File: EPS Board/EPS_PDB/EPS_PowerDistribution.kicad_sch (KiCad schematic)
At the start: 26 parts, among them U10 TPS259621DDAT, U11 LTC3624IDD-25PBF, U12 TPS259621DDAT, U13 TPS259621DDAT, U6 TPS259621DDAT, U7 TPS259621DDAT, U9 TPS259621DDAT

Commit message: Power Distri & Reg Schematic Complete
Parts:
- added C23, C24: 10uF, Capacitor_SMD:C_0805_2012Metric_Pad1.18x1.45mm_HandSolder, symbol Device:C_Small
- added C25, C27, C28: TBD, Capacitor_SMD:C_0805_2012Metric_Pad1.18x1.45mm_HandSolder, symbol Device:C_Small
- added C26: 0.47uF, Capacitor_SMD:C_0805_2012Metric_Pad1.18x1.45mm_HandSolder, symbol Device:C_Small
- added D3: D, symbol Device:D
- added JP2, JP3: ~, symbol Jumper:Jumper_3_Bridged12
- added L3: 16uH, Inductor_SMD:L_0805_2012Metric_Pad1.15x1.40mm_HandSolder, symbol Device:L
- added R29: 510, Resistor_SMD:R_0603_1608Metric_Pad0.98x0.95mm_HandSolder, symbol EPS_Schematic_v2-eagle-import:R-USCHIP-0805(2012-METRIC)
- added R30: 2.2k, Resistor_SMD:R_0603_1608Metric_Pad0.98x0.95mm_HandSolder, symbol EPS_Schematic_v2-eagle-import:R-USCHIP-0805(2012-METRIC)
- added R31: 10k, Resistor_SMD:R_0603_1608Metric_Pad0.98x0.95mm_HandSolder, symbol EPS_Schematic_v2-eagle-import:R-USCHIP-0805(2012-METRIC)
- added R32: 400k, Resistor_SMD:R_0603_1608Metric_Pad0.98x0.95mm_HandSolder, symbol EPS_Schematic_v2-eagle-import:R-USCHIP-0805(2012-METRIC)
- added R33: TBD, Resistor_SMD:R_0603_1608Metric_Pad0.98x0.95mm_HandSolder, symbol EPS_Schematic_v2-eagle-import:R-USCHIP-0805(2012-METRIC)
- added R34: 10, Resistor_SMD:R_0603_1608Metric_Pad0.98x0.95mm_HandSolder, symbol EPS_Schematic_v2-eagle-import:R-USCHIP-0805(2012-METRIC)
- added R35: 130k, Resistor_SMD:R_0603_1608Metric_Pad0.98x0.95mm_HandSolder, symbol EPS_Schematic_v2-eagle-import:R-USCHIP-0805(2012-METRIC)
- added R36: 15k, Resistor_SMD:R_0603_1608Metric_Pad0.98x0.95mm_HandSolder, symbol EPS_Schematic_v2-eagle-import:R-USCHIP-0805(2012-METRIC)
- added U14, U15, U16: TPS259621DDAT, EPS_Schematic_v2:IC_TPS259621DDAT, symbol TPS259621DDAT:TPS259621DDAT
- added U17: LM5000-3MTCX, LM5000-3MTCX:SOP65P640X120-16N, symbol LM5000-3MTCX:LM5000-3MTCX
- R14: value 510 -> 560
- R18, R21: value R-USCHIP-0805(2012-METRIC) -> 560
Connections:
- net ADCS_3.3V_EN is gone; now on net 3.3V_bus: U13.3 (EN/UVLO)
- net 12V_bus: now also C28.2, D3.1 (K), R35.1
- net 3.3V_bus: now also U8.8 (FB), U15.4 (IN), U16.4 (IN)
- net 5V_bus: now also U14.4 (IN)
- net GND: now also U8.11 (GND), U8.12 (GND), C23.1, C24.1, C26.1, C27.1, C28.1, JP2.1 (A), JP3.1 (A), R29.1, R30.1, R31.1, R32.2, R33.2, R36.1, U14.1 (GND), U14.9 (EXP), U15.1 (GND), U15.8 (OVCSEL), U15.9 (EXP), U16.1 (GND), U16.8 (OVCSEL), U16.9 (EXP), U17.16 (TEST), U17.4 (AGND), U17.5 (PGND-1), U17.6 (PGND), U17.7 (PGND-3), U17.8 (PGND-2); no longer C19.1
- net at C22.2, U11.6 (INTVCC): now also JP2.3 (B)
- net at U11.7 (MODE/SYNC): now also JP2.2 (C)
- net at L1.2: now also U8.1 (SW), U8.2 (SW)
- net at C17.2: now also U8.9 (INTVCC), JP3.3 (B)
- net VBUS: now reaches C21.1
- net VBUS: now also C19.1, L3.1, R34.2
- net at C19.2: now also U8.3 (Vin), U8.4 (Vin), U8.5 (RUN)
- net at U8.10 (MODE/SYNC): now also JP3.2 (C)
- net 3V3_STATUS: now reaches U8.6 (PGOOD)
- net 5V_PGOOD renamed 5V_STATUS
- net ADCS_12V renamed 12V_ADCS
- net ADCS_12V_EN renamed EN_12V_ADCS
- net ADCS_12V_FLT renamed FLT_12V_ADCS
- net ADCS_3.3V renamed 3V3_EPS
- net ADCS_3.3V_FLT renamed FLT_3V3_EPS
- net ADCS_5V renamed 5V_ADCS
- net ADCS_5V_EN renamed EN_5V_ADCS
- net ADCS_5V_FLT renamed FLT_5V_ADCS
- net COMM_5V renamed 5V_COMM
- net COMM_5V_EN renamed EN_5V_COMM
- net COMM_5V_FLT renamed FLT_5V_COMM
- net EPS_5V renamed 5V_EPS
- net EPS_5V_EN renamed EN_5V_EPS
- net EPS_5V_FLT renamed FLT_5V_EPS
- net OBC_5V renamed 5V_OBC
- net OBC_5V_EN renamed EN_5V_OBC
- net OBC_5V_FLT renamed FLT_5V_OBC
- new net: C25.1, R33.1
- new net: C24.2, C25.2, U17.1 (COMP)
- new net: R35.2, R36.2, U17.2 (FB)
- new net: R32.1, U14.8 (OVCSEL)
- new net: R30.2, U15.7 (ILM)
- new net: D3.2 (A), L3.2, U17.10 (SW), U17.11 (SW-2), U17.9 (SW-1)
- new net: C23.2, U17.12 (BYP)
- new net: C26.2, R34.1, U17.13 (VIN)
- new net: C27.2, U17.14 (SS)
- new net: R29.2, U14.7 (ILM)
- new net: R31.2, U16.7 (ILM)
- new net 12V_SHDN: U17.3 (SHDN)
- new net 3V3_ADCS: U15.5 (OUT)
- new net 3V3_ANT: U16.5 (OUT)
- new net 5V_PAY: U14.5 (OUT)
- new net EN_3V3_ADCS: U15.3 (EN/UVLO)
- new net EN_3V3_ANT: U16.3 (EN/UVLO)
- new net EN_5V_PAY: U14.3 (EN/UVLO)
- new net FLT_3V3_ADCS: U15.6 (~{FLT})
- new net FLT_3V3_ANT: U16.6 (~{FLT})
- new net FLT_5V_PAY: U14.6 (~{FLT})
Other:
- moved on the sheet: C17, C18, C19, C20, C21, C22, L1, L2, R13, R14, R15, R16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

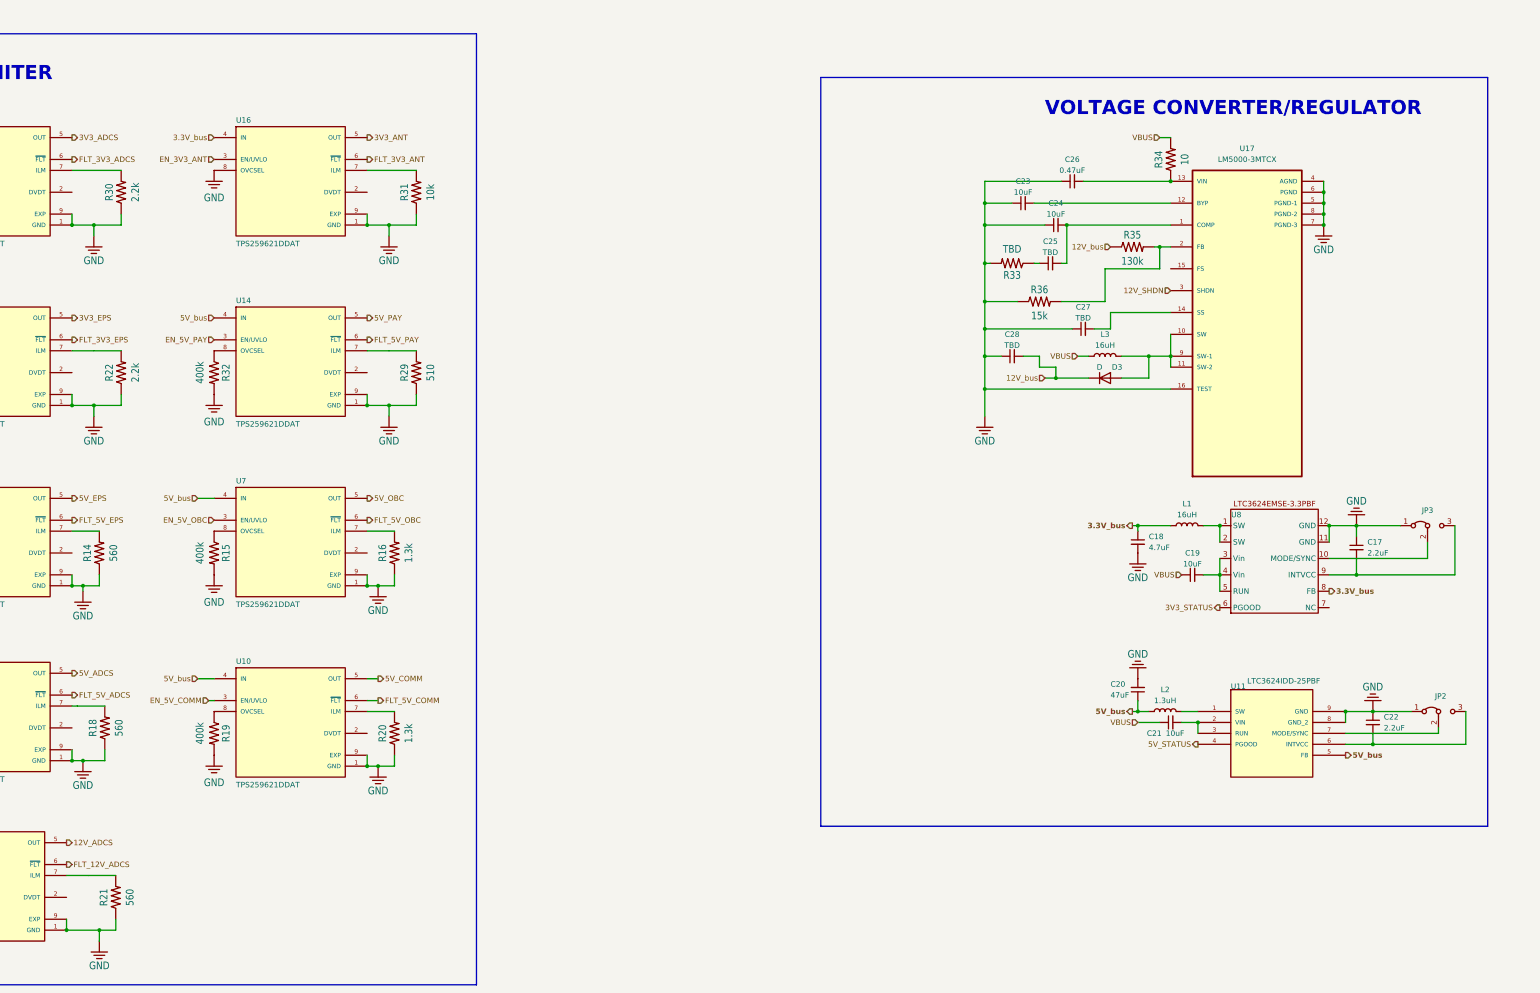
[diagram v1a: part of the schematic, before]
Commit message: Added ADC to schematic
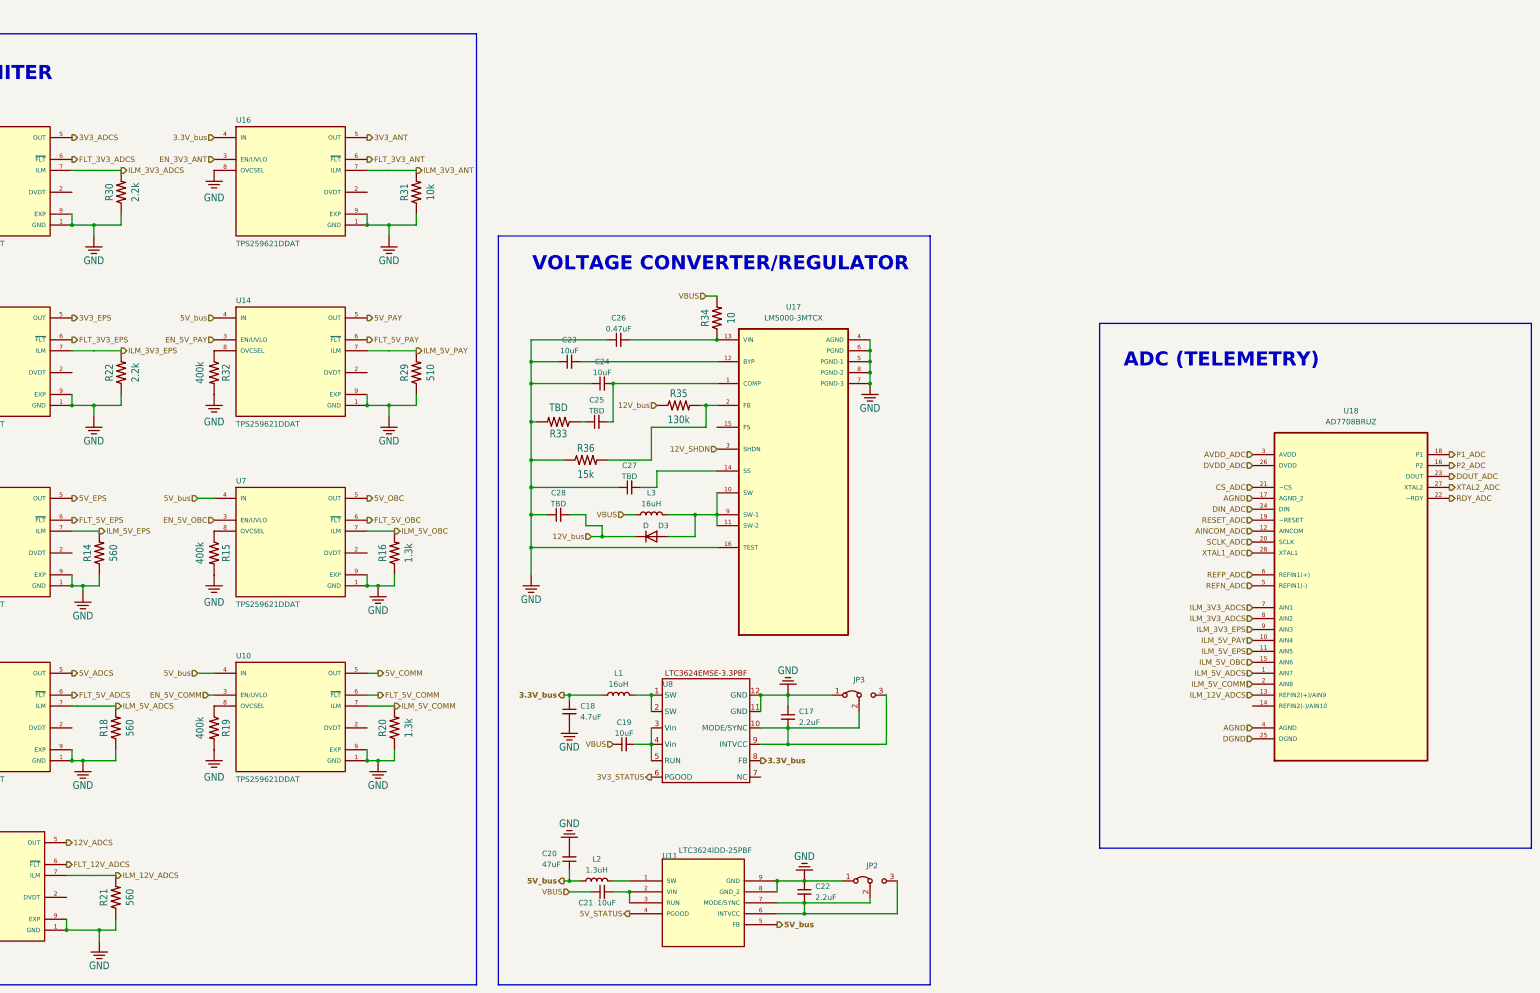
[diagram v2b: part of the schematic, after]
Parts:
- added U18: AD7708BRUZ, AD7708BRUZ:SOP65P638X110-28N, symbol AD7708BRUZ:AD7708BRUZ
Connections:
- net ILM_5V_OBC: now reaches R16.2, U7.7 (ILM)
- net ILM_5V_OBC: now also U18.15 (AIN6)
- net at C22.2, JP2.3 (B), U11.6 (INTVCC): now also JP2.2 (C), U11.7 (MODE/SYNC)
- net ILM_5V_ADCS: now reaches R18.2, U9.7 (ILM)
- net ILM_5V_ADCS: now also U18.1 (AIN7)
- net ILM_3V3_ADCS: now reaches R30.2, U15.7 (ILM)
- net ILM_3V3_ADCS: now also U18.7 (AIN1), U18.8 (AIN2)
- net ILM_12V_ADCS: now reaches R21.2, U12.7 (ILM)
- net ILM_12V_ADCS: now also U18.13 (REFIN2(+)/AIN9)
- net ILM_3V3_EPS: now reaches R22.2, U13.7 (ILM)
- net ILM_3V3_EPS: now also U18.9 (AIN3)
- net at C17.2, JP3.3 (B), U8.9 (INTVCC): now also JP3.2 (C), U8.10 (MODE/SYNC)
- net ILM_5V_EPS: now reaches R14.2, U6.7 (ILM)
- net ILM_5V_EPS: now also U18.11 (AIN5)
- net ILM_5V_PAY: now reaches R29.2, U14.7 (ILM)
- net ILM_5V_PAY: now also U18.10 (AIN4)
- net ILM_5V_COMM: now reaches R20.2, U10.7 (ILM)
- net ILM_5V_COMM: now also U18.2 (AIN8)
- net ILM_3V3_ANT: now reaches R31.2, U16.7 (ILM)
- new net AGND: U18.17 (AGND_2), U18.4 (AGND)
- new net AINCOM_ADC: U18.12 (AINCOM)
- new net AVDD_ADC: U18.3 (AVDD)
- new net CS_ADC: U18.21 (~CS)
- new net DGND: U18.25 (DGND)
- new net DIN_ADC: U18.24 (DIN)
- new net DOUT_ADC: U18.23 (DOUT)
- new net DVDD_ADC: U18.26 (DVDD)
- new net P1_ADC: U18.18 (P1)
- new net P2_ADC: U18.16 (P2)
- new net RDY_ADC: U18.22 (~RDY)
- new net REFN_ADC: U18.5 (REFIN1(-))
- new net REFP_ADC: U18.6 (REFIN1(+))
- new net RESET_ADC: U18.19 (~RESET)
- new net SCLK_ADC: U18.20 (SCLK)
- new net XTAL1_ADC: U18.28 (XTAL1)
- new net XTAL2_ADC: U18.27 (XTAL2)
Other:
- note added: "ADC (TELEMETRY)"
- moved on the sheet: C17, C18, C19, C20, C21, C22, C23, C24, C25, C26, C27, C28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

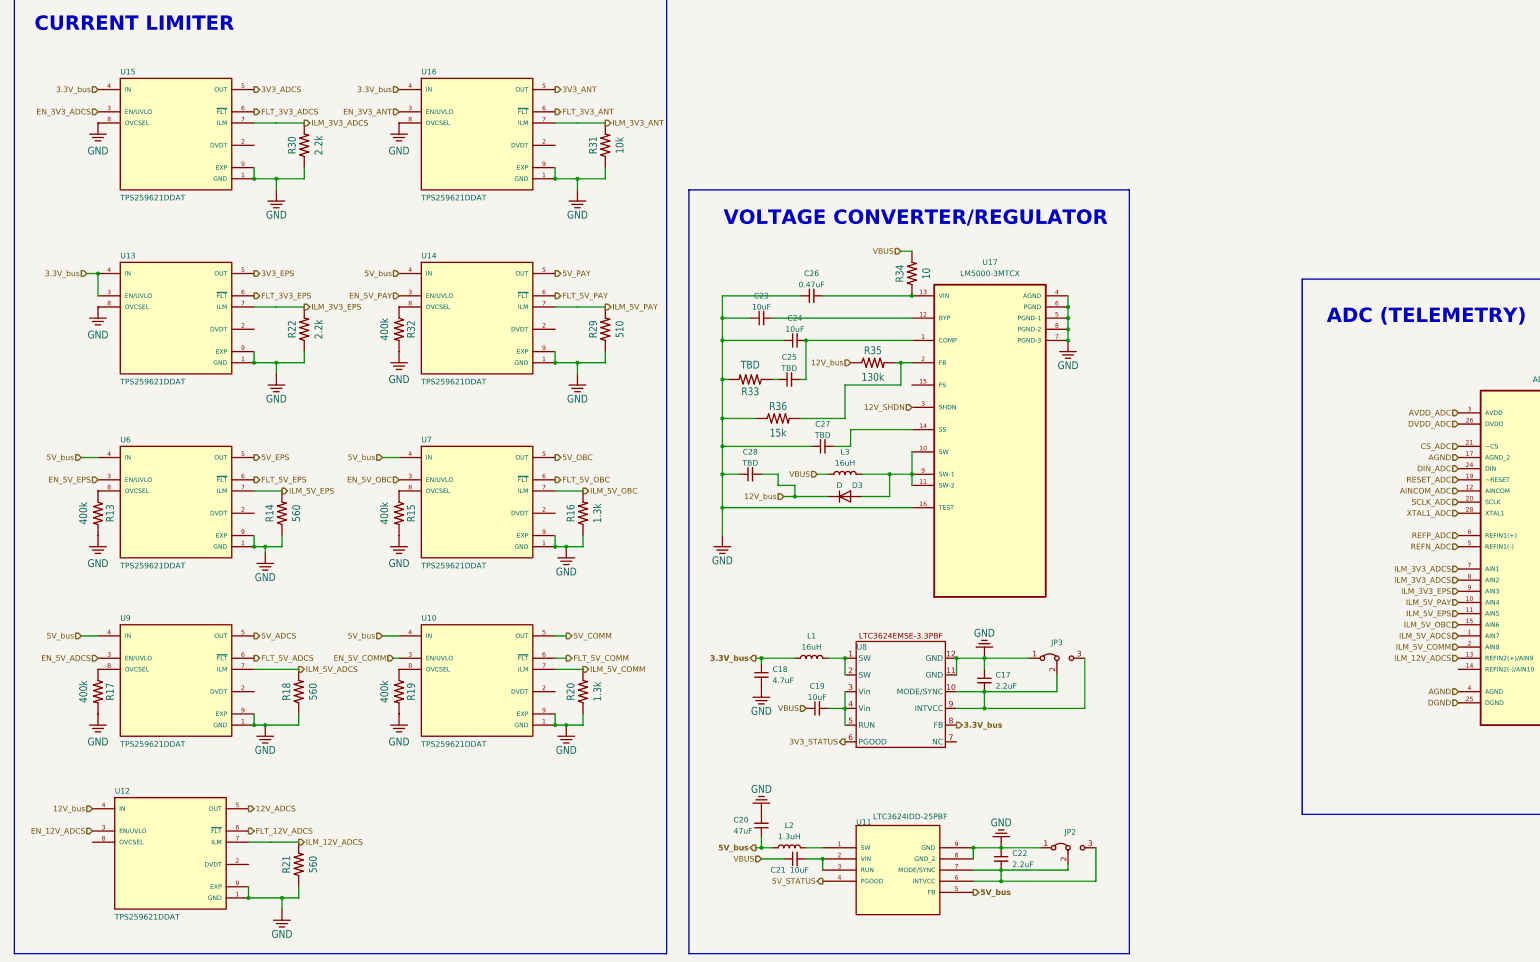
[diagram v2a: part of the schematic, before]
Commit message: Updated labels from nets
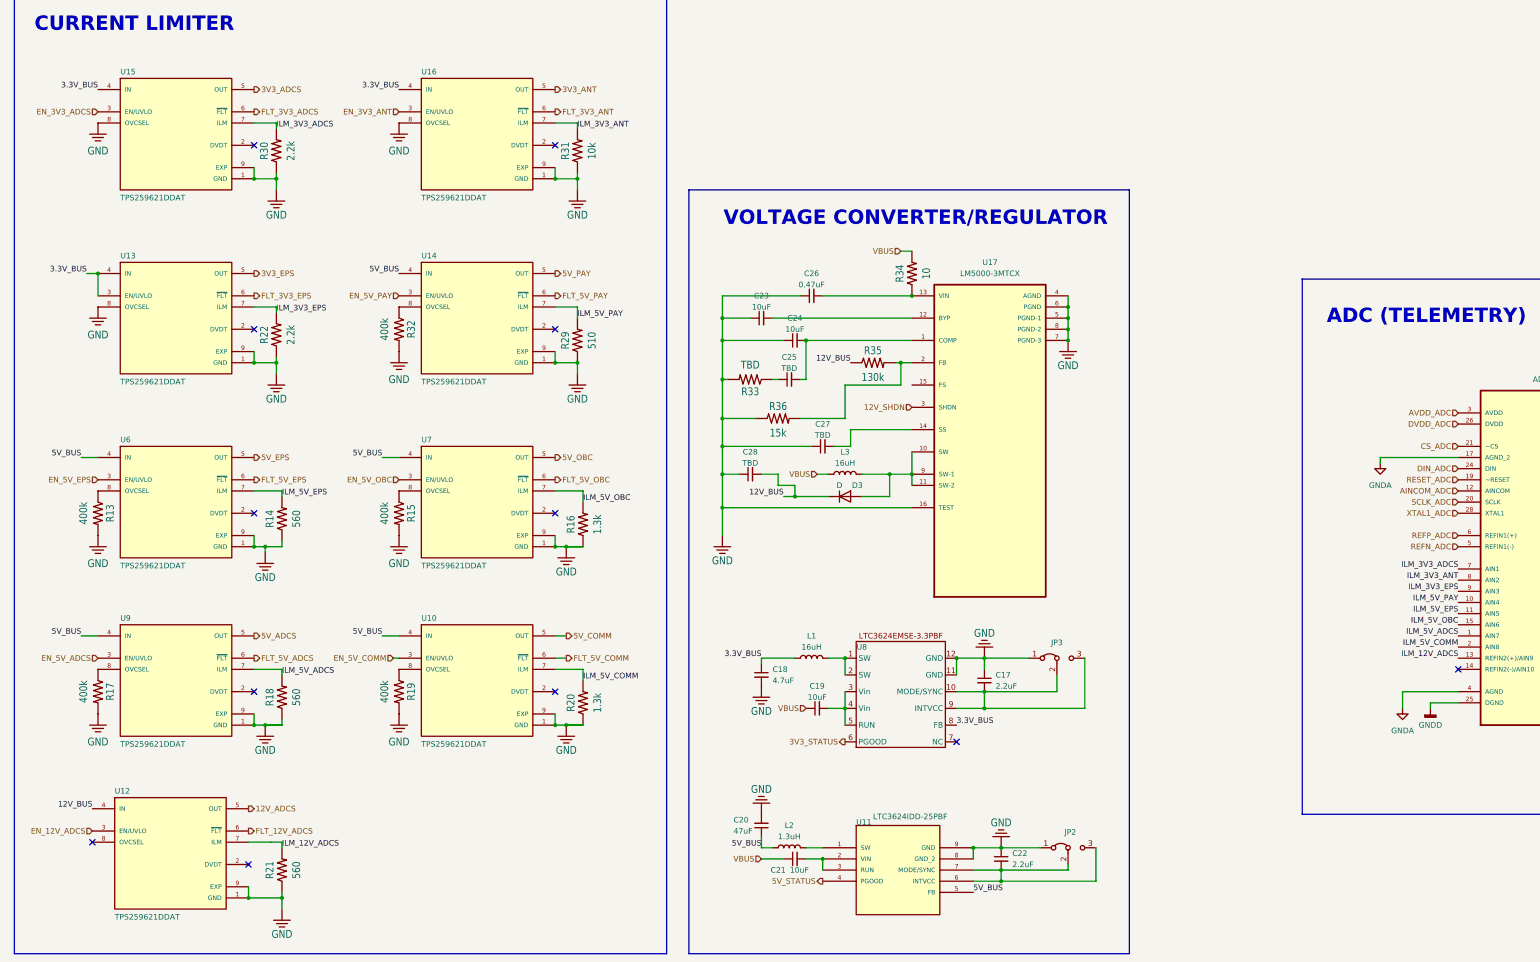
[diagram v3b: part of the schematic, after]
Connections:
- net ILM_3V3_ADCS: no longer U18.8 (AIN2)
- net ILM_3V3_ANT: now also U18.8 (AIN2)
- net 12V_bus renamed 12V_BUS
- net 3.3V_bus renamed 3.3V_BUS
- net 5V_bus renamed 5V_BUS
- net AGND renamed GNDA
- net DGND renamed GNDD
- no-connect marks 0 -> 12
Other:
- moved on the sheet: R14, R16, R18, R20, R21, R22, R29, R30, R31
